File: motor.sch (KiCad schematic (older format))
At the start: 44 parts, among them J16 70543-0003, Q10 PMPB20EN, Q3 PMPB20EN, Q4 PMPB20EN, Q5 PMPB20EN, Q6 PMPB20EN, Q7 PMPB20EN, Q8 PMPB20EN, Q9 PMPB20EN, U6 TMC2160-TA

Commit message: Complete functional design
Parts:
- renumbered C34 to C29, C35 to C30, C36 to C31, C37 to C32, C38 to C33, C39 to C34, C40 to C35, C41 to C36, C42 to C37, C43 to C38, C44 to C39, C45 to C40, C46 to C41, C47 to C42, C48 to C43, C49 to C44, D21 to D7, J16 to J5, R21 to R13, R22 to R14, R23 to R15, R24 to R16, R25 to R17, R26 to R18, R27 to R19, R28 to R20, R29 to R21, R30 to R22, R31 to R23, R32 to R24, R33 to R25, R34 to R26, R35 to R27, R36 to R28, R37 to R29

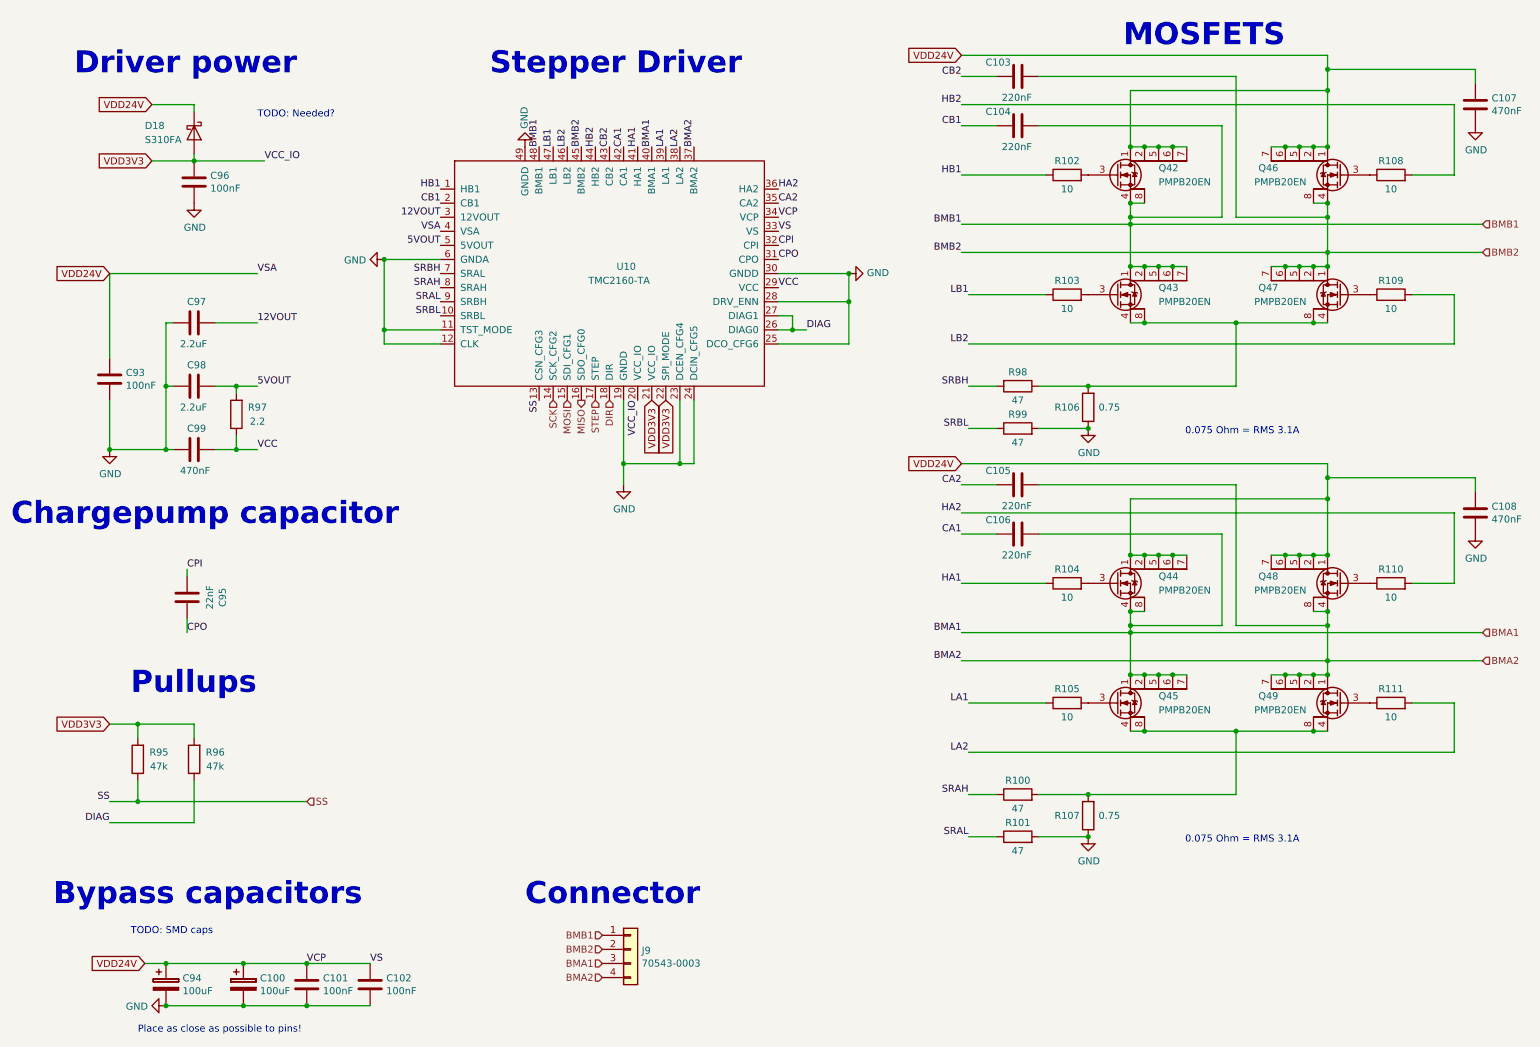
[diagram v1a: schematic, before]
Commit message: Finish silkscreen and updated README.md
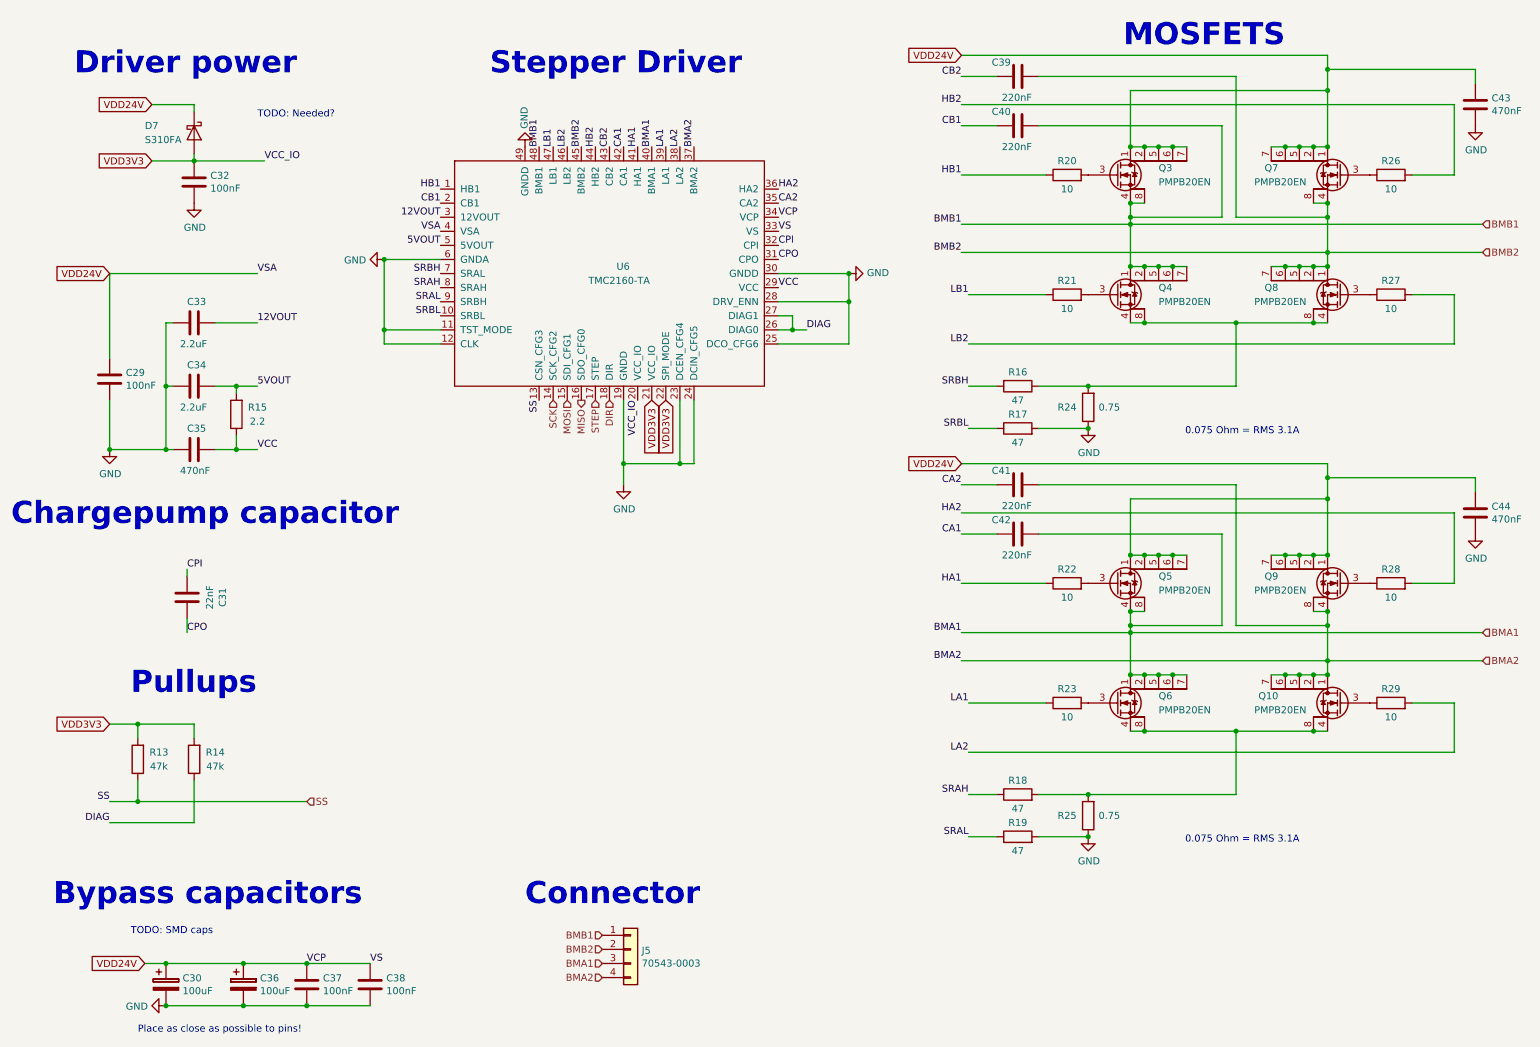
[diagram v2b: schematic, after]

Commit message: Change default SOT1220 MOSFET and added parts alternatives
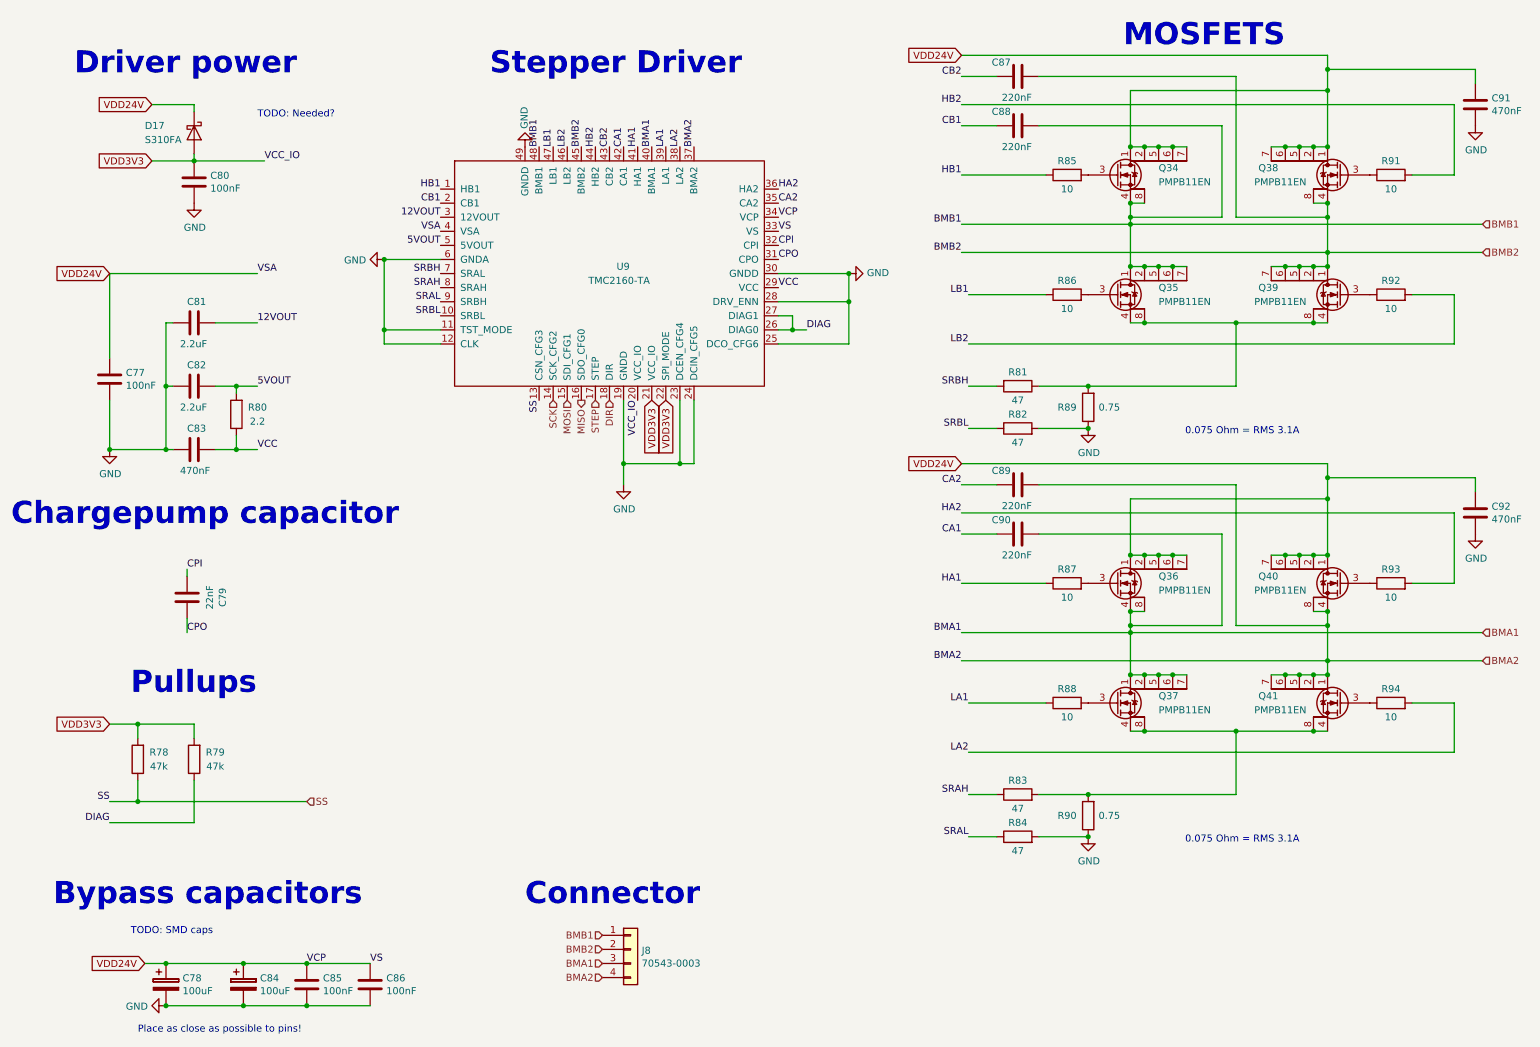
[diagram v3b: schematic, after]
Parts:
- Q10, Q3, Q4, Q5, Q6, Q7, Q8, Q9: value PMPB20EN -> PMPB11EN

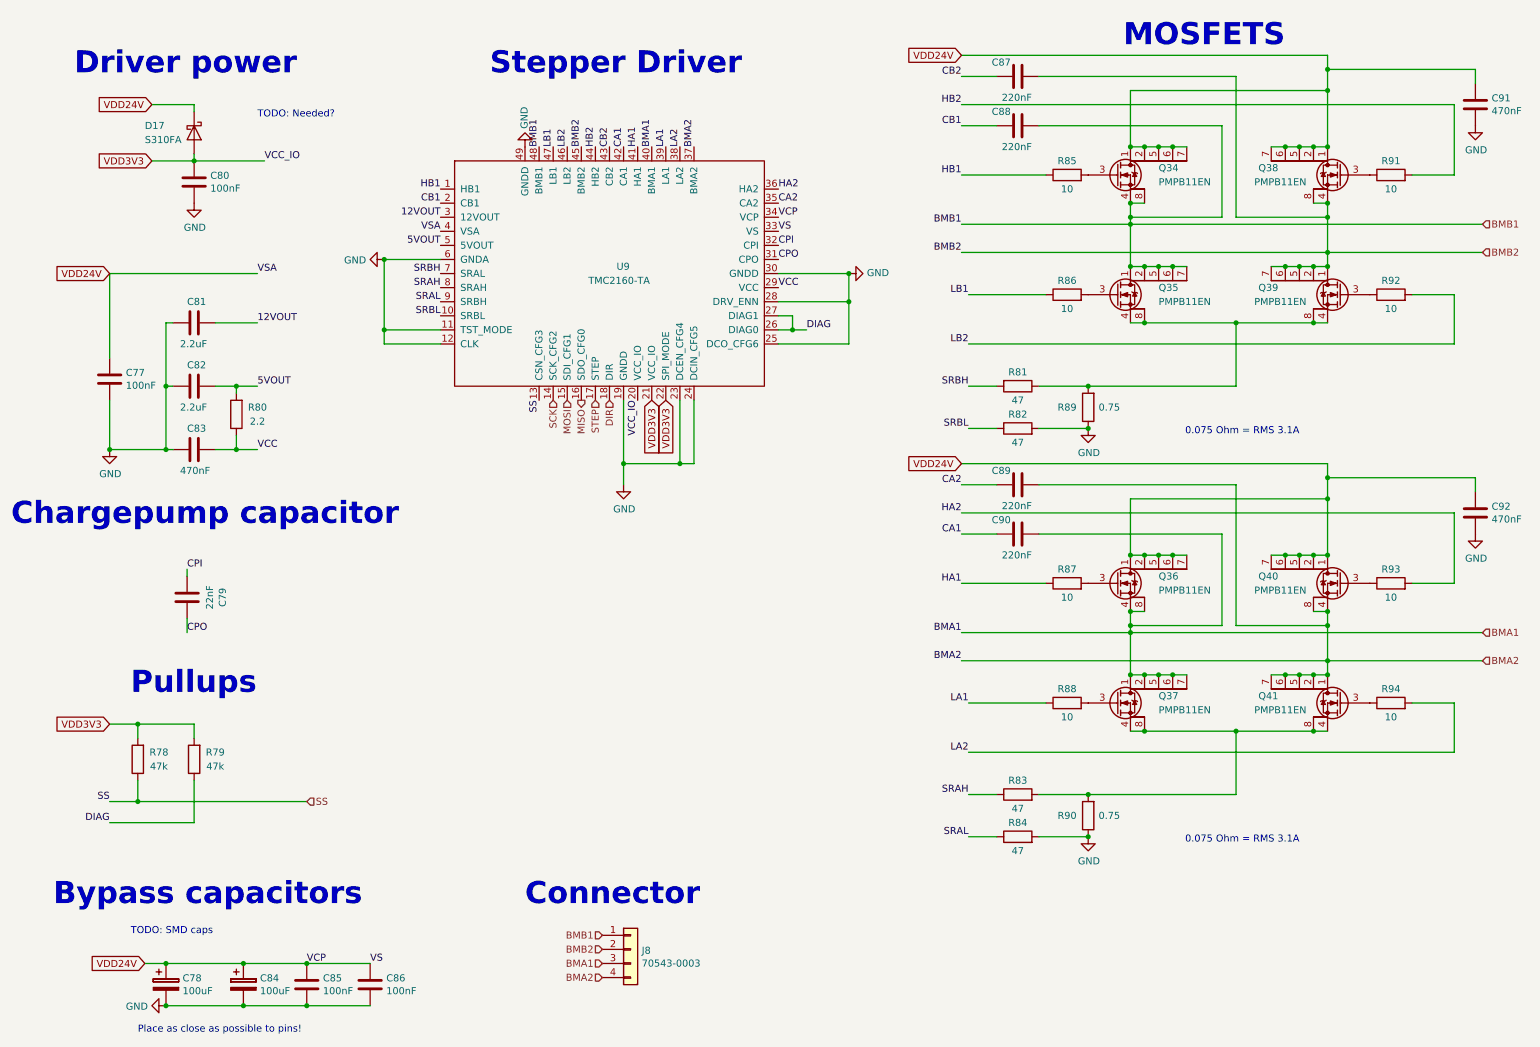
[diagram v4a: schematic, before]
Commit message: Add bypass cap for I2C EEPROMs and redone some copper pour
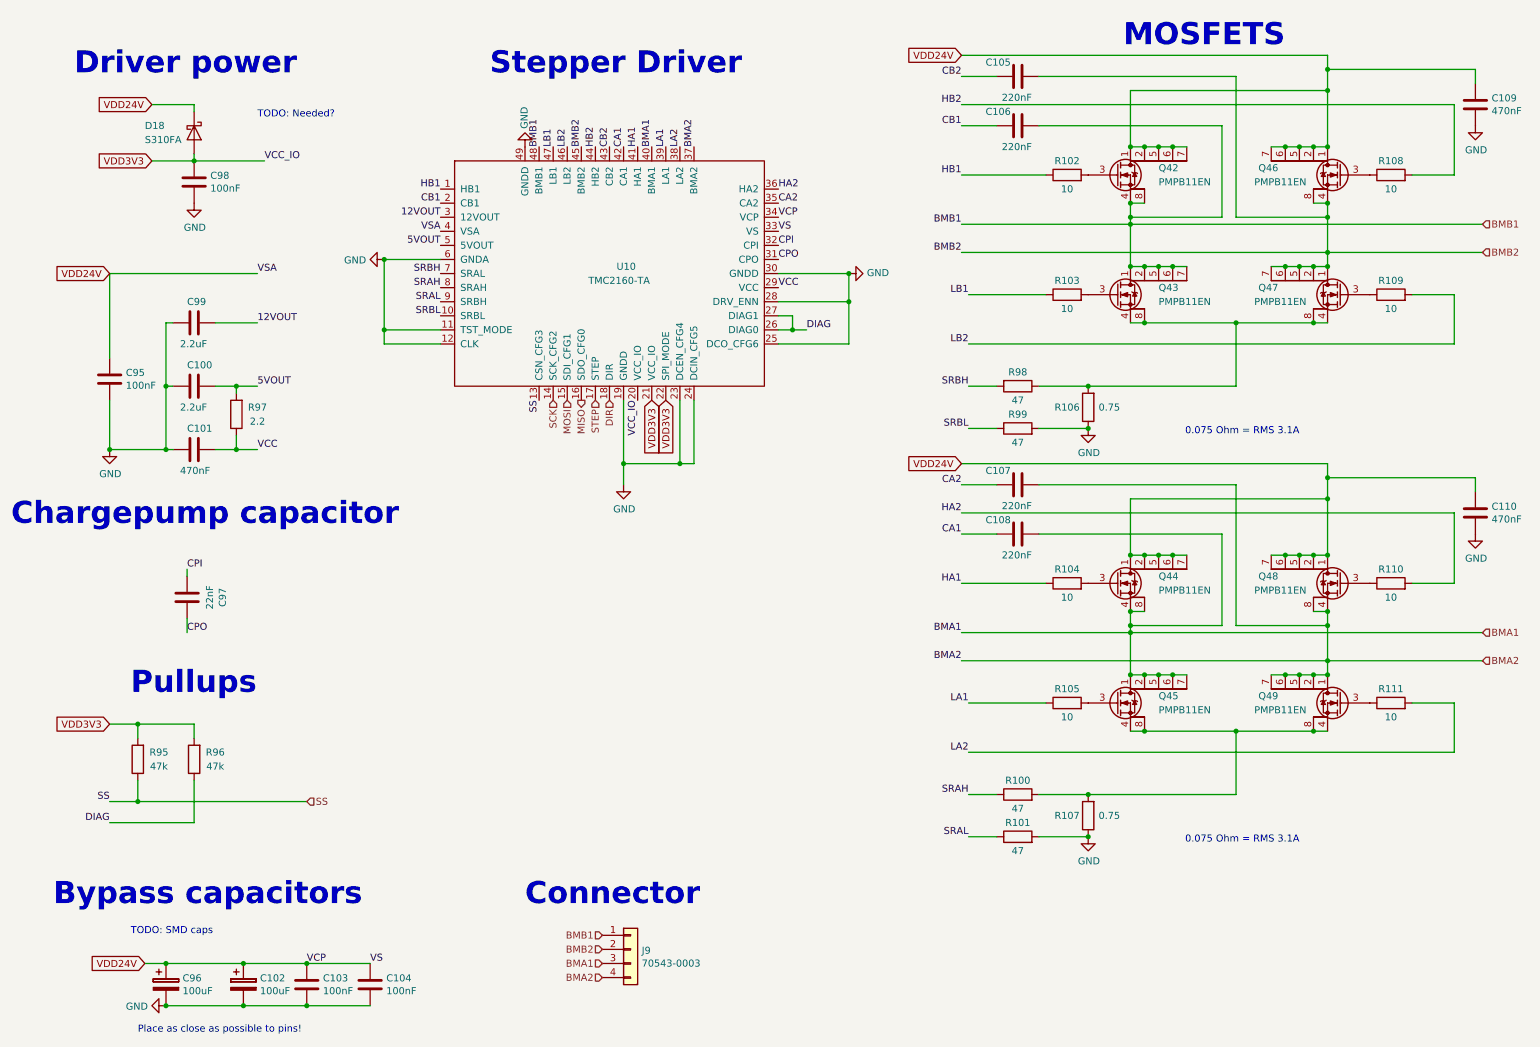
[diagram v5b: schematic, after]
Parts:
- renumbered C29 to C31, C30 to C32, C31 to C33, C32 to C34, C33 to C35, C34 to C36, C35 to C37, C36 to C38, C37 to C39, C38 to C40, C39 to C41, C40 to C42, C41 to C43, C42 to C44, C43 to C45, C44 to C46

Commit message: Fix MOSFET selection
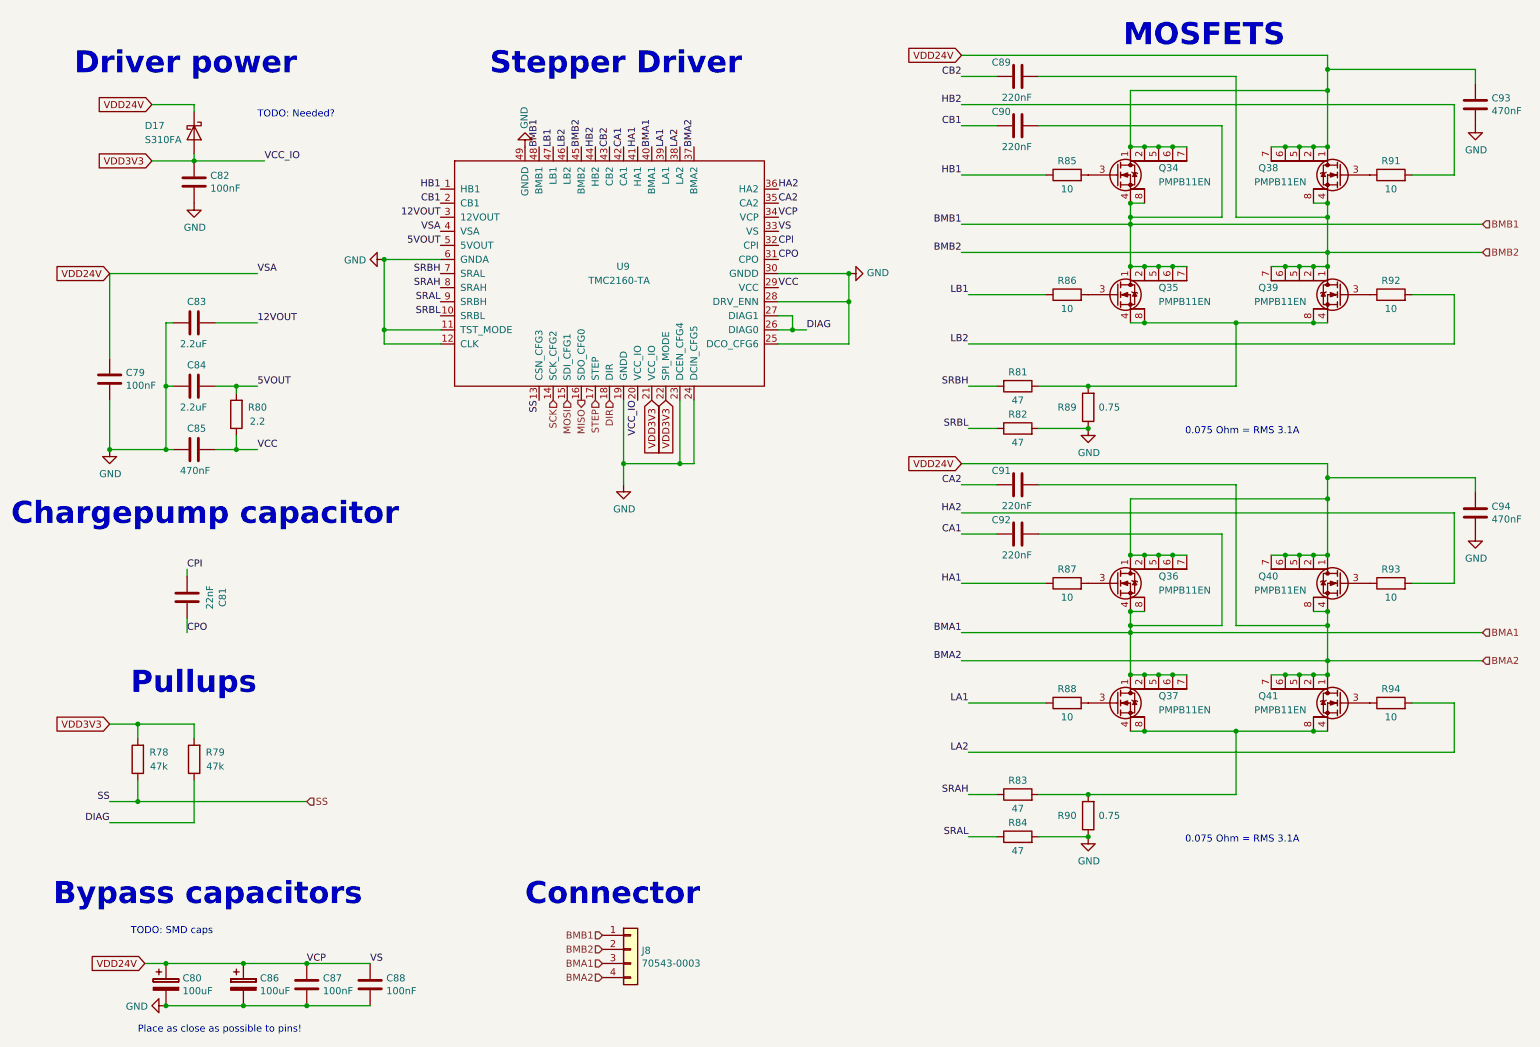
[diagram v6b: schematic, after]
